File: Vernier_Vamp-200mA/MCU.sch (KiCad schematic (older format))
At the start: 11 parts

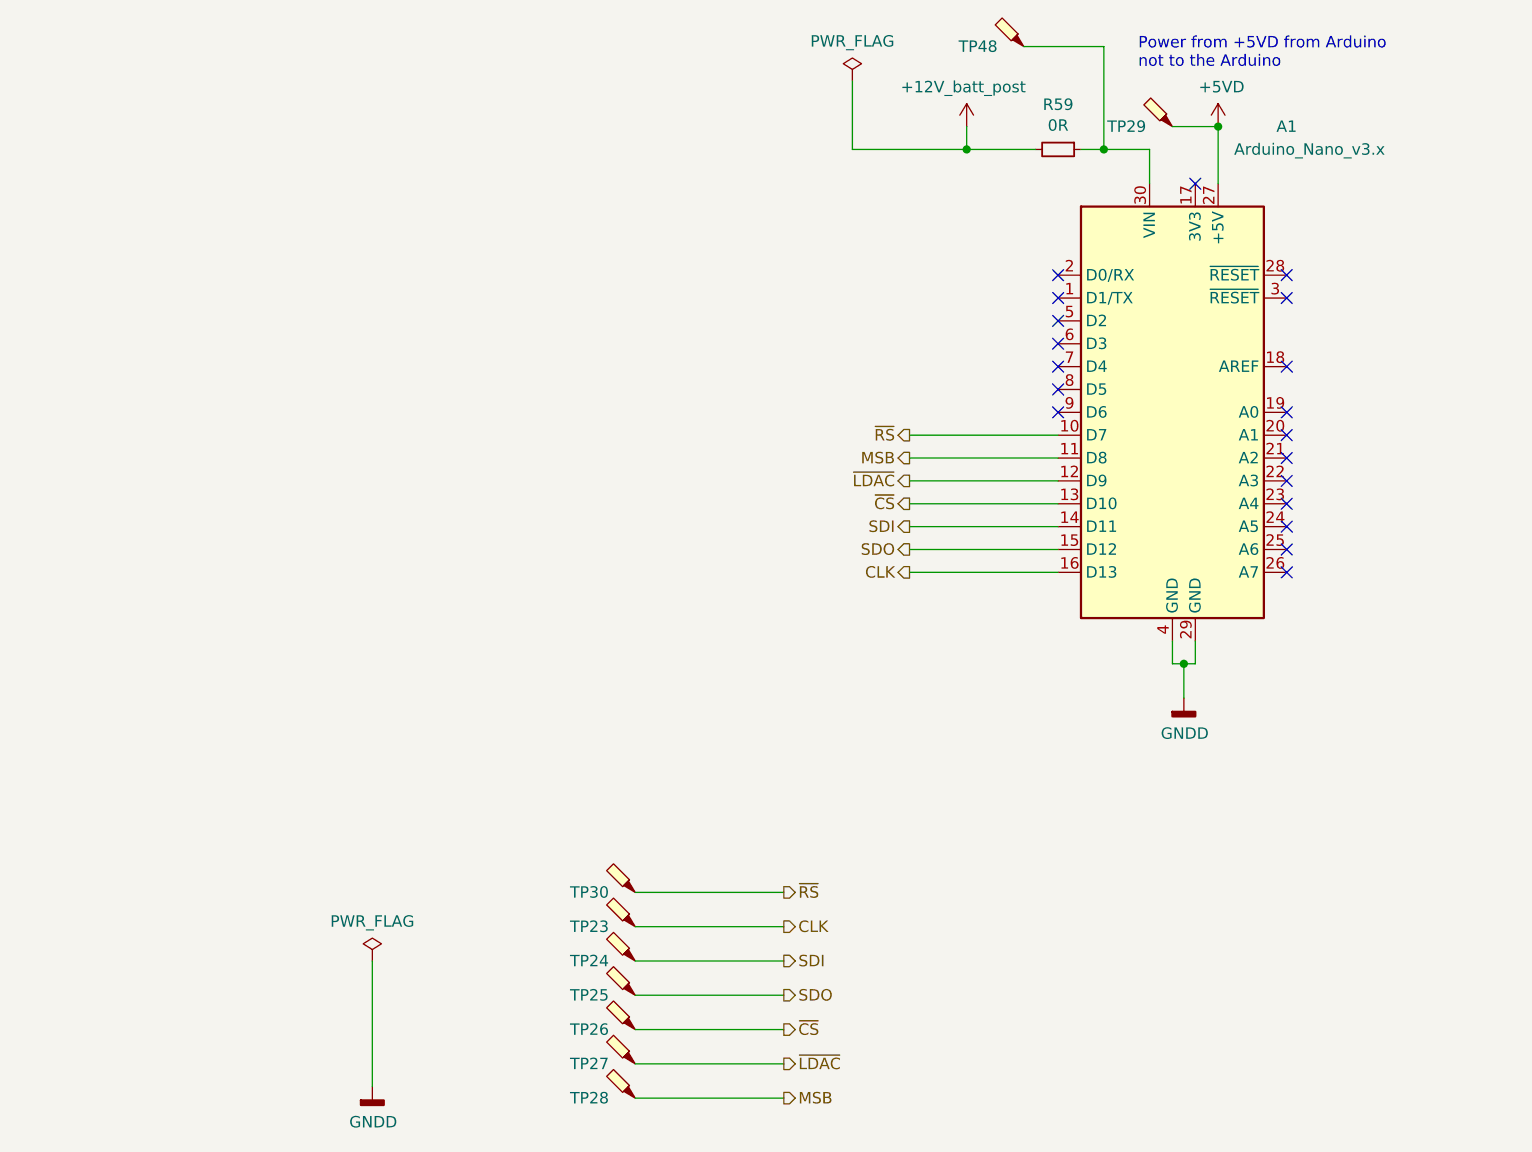
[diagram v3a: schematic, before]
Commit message: 1.0D Update
LCCD changes
-Addition of trigger for calibration
-PCB optimisation

HCCD changes
-New output stage designed
-Changes from 1.0C applied to HCCD
-New more optimised layout
-New shielding over analog section
-Addition of trigger for calibration

New symbols and footprint creation
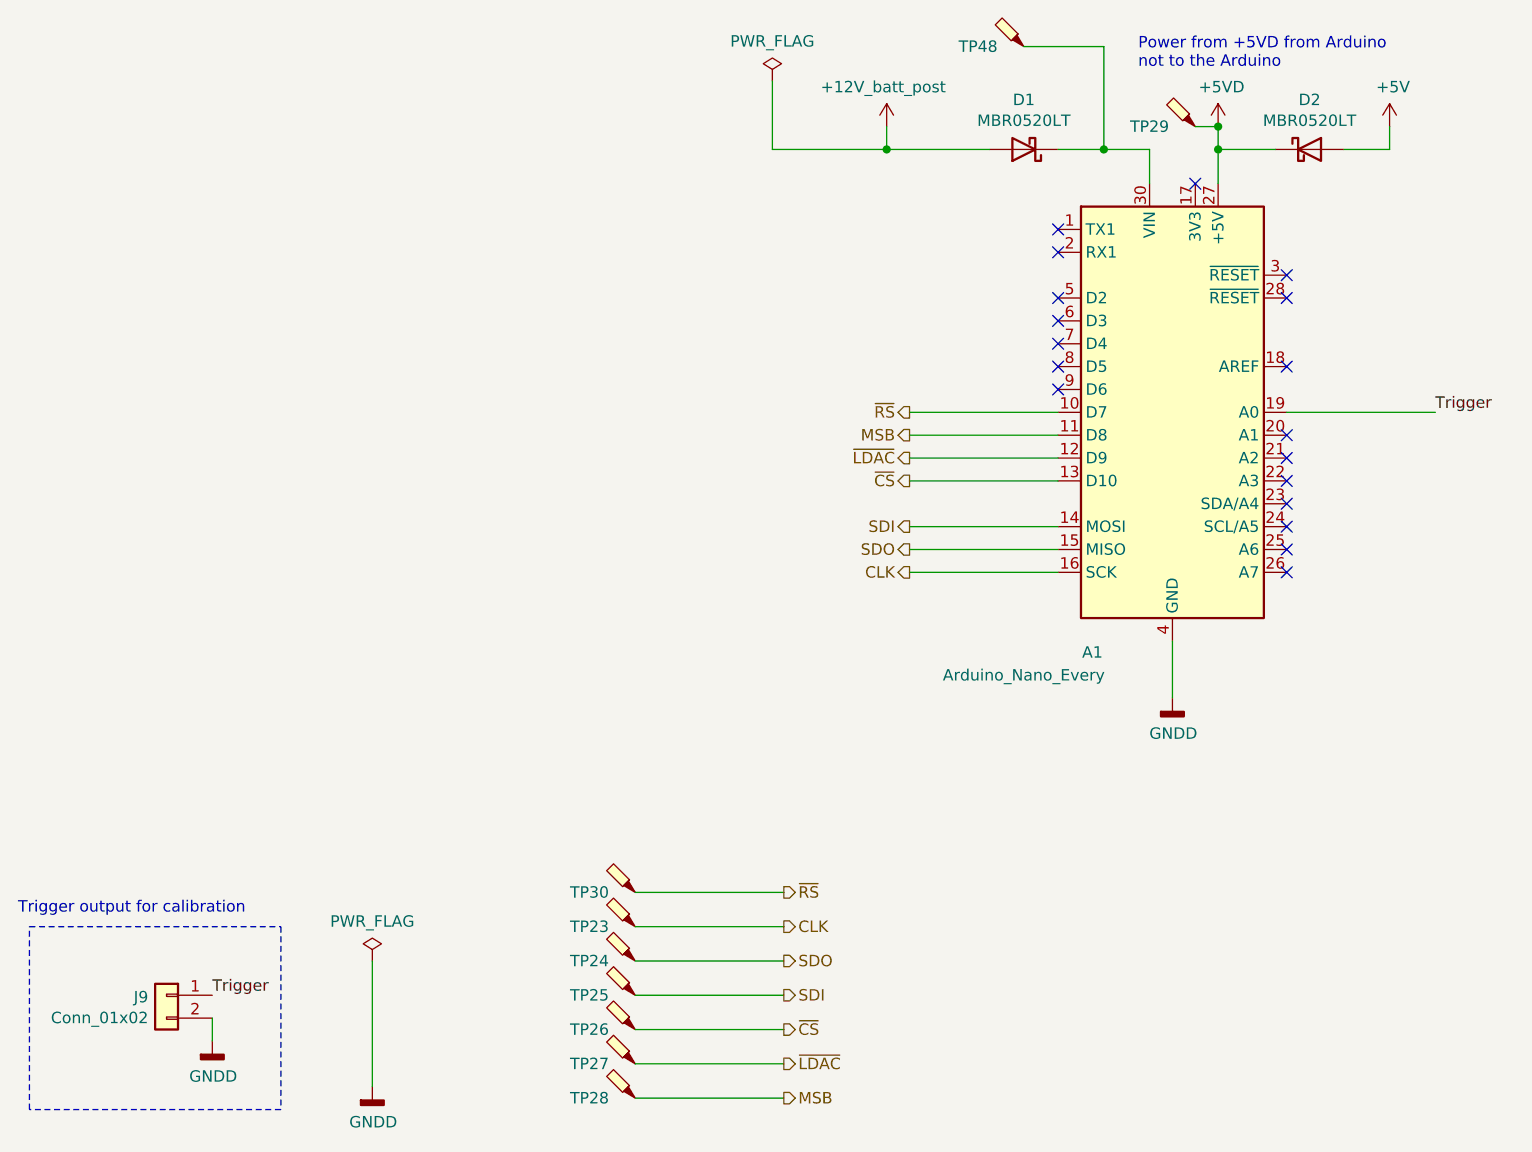
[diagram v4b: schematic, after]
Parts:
- removed A1: Arduino_Nano_v3.x, Module:Arduino_Nano, symbol MCU_Module:Arduino_Nano_v3.x
- removed R59: 0R, Resistor_SMD:R_0603_1608Metric_Pad1.05x0.95mm_HandSolder, symbol Device:R_Small
- added A1: Arduino_Nano_Every, Module:Arduino_Nano, symbol MCU_Module:Arduino_Nano_Every
- added D1, D2: MBR0520LT, Diode_SMD:D_SOD-123, symbol Diode:MBR0520LT
- added J9: Conn_01x02, Connector_PinHeader_2.54mm:PinHeader_1x02_P2.54mm_Vertical, symbol Connector_Generic:Conn_01x02
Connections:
- net +12V_batt_post: now also D1.2 (A)
- net +5VD: now also A1.27 (+5V), D2.1 (K)
- net CLK: now also A1.16 (SCK)
- net GNDD: now also A1.29 (GND), A1.4 (GND), J9.2 (Pin_2)
- net MSB: now also A1.11 (D8)
- net SDI: now also TP25.1, A1.14 (MOSI); no longer TP24.1
- net SDO: now also TP24.1, A1.15 (MISO); no longer TP25.1
- net ~CS: now also A1.13 (D10)
- net ~LDAC: now also A1.12 (D9)
- net ~RS: now also A1.10 (D7)
- net at TP48.1: now also A1.30 (VIN), D1.1 (K)
- new net +5V: D2.2 (A)
- new net Trigger: A1.19 (A0), J9.1 (Pin_1)
- no-connect marks 19 -> 18
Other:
- note added: "Trigger output for calibration"
- moved on the sheet: TP29
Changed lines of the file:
@@
 $Descr A4 11693 8268
 encoding utf-8
-Sheet 5 7
-Title "\"Vernier Vamp\" Coil Driver - 200mA"
+Sheet 4 7
+Title "\"Vernier Vamp\" Coil Driver - HCCD"
 Date "2020-04-27"
-Rev "1.0B"
+Rev "1.0D"
 Comp "Strathclyde University"
 Comment1 "Designed by: Marcin Mrozowski"
@@
 L power:GNDD #PWR0196
 U 1 1 5E449396
-P 5900 5050
+P 5850 5050
 AR Path="/5E1DEB8C/5E449396" Ref="#PWR0196"  Part="1"
 AR Path="/5E5EF2D7/5E449396" Ref="#PWR?"  Part="1"
-F 0 "#PWR0196" H 5900 4800 50  0001 C CNN
-F 1 "GNDD" H 5904 4895 50  0000 C CNN
-F 2 "" H 5900 5050 50  0001 C CNN
-F 3 "" H 5900 5050 50  0001 C CNN
-	1    5900 5050
-	1    0    0    -1
-$EndComp
-Wire Wire Line
-	5850 4800 5850 4900
-Wire Wire Line
-	5850 4900 5900 4900
-Wire Wire Line
-	5950 4900 5950 4800
-Wire Wire Line
-	5900 4900 5900 5050
-Connection ~ 5900 4900
-Wire Wire Line
-	5900 4900 5950 4900
+F 0 "#PWR0196" H 5850 4800 50  0001 C CNN
+F 1 "GNDD" H 5854 4895 50  0000 C CNN
+F 2 "" H 5850 5050 50  0001 C CNN
+F 3 "" H 5850 5050 50  0001 C CNN
+	1    5850 5050
+	1    0    0    -1
+$EndComp
+Wire Wire Line
+	5850 4800 5850 5050
 Text HLabel 4700 4500 0    50   Output ~ 0
 CLK
-Text HLabel 4700 4200 0    50   Output ~ 0
+Text HLabel 4700 4100 0    50   Output ~ 0
 ~CS
 Text HLabel 4700 4300 0    50   Output ~ 0
@@
 	5350 4500 4700 4500
 Wire Wire Line
-	4700 4200 5350 4200
+	4700 4100 5350 4100
 Wire Wire Line
 	4700 4300 5350 4300
 Wire Wire Line
 	4700 4400 5350 4400
-NoConn ~ 5350 3700
-NoConn ~ 5350 3600
-NoConn ~ 5350 3500
-NoConn ~ 5350 3400
-NoConn ~ 6350 3600
-NoConn ~ 6350 3800
-NoConn ~ 6350 3900
-NoConn ~ 6350 4000
-NoConn ~ 6350 4100
-NoConn ~ 6350 4200
-NoConn ~ 6350 4300
-NoConn ~ 6350 4400
-NoConn ~ 6350 4500
-Text HLabel 4700 4100 0    50   Output ~ 0
+Text HLabel 4700 4000 0    50   Output ~ 0
 ~LDAC
-Text HLabel 4700 4000 0    50   Output ~ 0
+Text HLabel 4700 3900 0    50   Output ~ 0
 MSB
-NoConn ~ 5350 3800
-Wire Wire Line
-	4700 4000 5350 4000
-Wire Wire Line
-	5350 4100 4700 4100
-Text HLabel 4700 3900 0    50   Output ~ 0
+Wire Wire Line
+	4700 3900 5350 3900
+Wire Wire Line
+	5350 4000 4700 4000
+Text HLabel 4700 3800 0    50   Output ~ 0
 ~RS
-NoConn ~ 5350 3200
-NoConn ~ 5350 3300
 NoConn ~ 5950 2800
 $Comp
@@
 Text HLabel 4150 6500 2    50   Output ~ 0
 ~CS
+Text HLabel 4150 6350 2    50   Output ~ 0
+SDI
 Text HLabel 4150 6200 2    50   Output ~ 0
-SDI
-Text HLabel 4150 6350 2    50   Output ~ 0
 SDO
 Wire Wire Line
@@
 	4150 6500 3500 6500
 Wire Wire Line
+	4150 6350 3500 6350
+Wire Wire Line
 	4150 6200 3500 6200
-Wire Wire Line
-	4150 6350 3500 6350
 Text HLabel 4150 6650 2    50   Output ~ 0
 ~LDAC
@@
 L Connector:TestPoint_Probe TP29
 U 1 1 62363521
-P 5850 2550
-F 0 "TP29" V 5850 2750 50  0000 C CNN
-F 1 "TestPoint_Probe" V 6049 2605 50  0001 C CNN
-F 2 "TestPoint:TestPoint_Pad_D1.0mm" H 6050 2550 50  0001 C CNN
-F 3 "~" H 6050 2550 50  0001 C CNN
-	1    5850 2550
-	0    -1   -1   0
-$EndComp
-Wire Wire Line
-	6050 2550 5850 2550
+P 5950 2550
+F 0 "TP29" V 5950 2750 50  0000 C CNN
+F 1 "TestPoint_Probe" V 6149 2605 50  0001 C CNN
+F 2 "TestPoint:TestPoint_Pad_D1.0mm" H 6150 2550 50  0001 C CNN
+F 3 "~" H 6150 2550 50  0001 C CNN
+	1    5950 2550
+	0    -1   -1   0
+$EndComp
+Wire Wire Line
+	6050 2550 5950 2550
 Connection ~ 6050 2550
-$Comp
-L MCU_Module:Arduino_Nano_v3.x A1
-U 1 1 5E447129
-P 5850 3800
-AR Path="/5E1DEB8C/5E447129" Ref="A1"  Part="1"
-AR Path="/5E5EF2D7/5E447129" Ref="A?"  Part="1"
-F 0 "A1" H 6350 5050 50  0000 C CNN
-F 1 "Arduino_Nano_v3.x" H 6450 4950 50  0000 C CNN
-F 2 "Module:Arduino_Nano" H 5850 3800 50  0001 C CIN
-F 3 "http://www.mouser.com/pdfdocs/Gravitech_Arduino_Nano3_0.pdf" H 5850 3800 50  0001 C CNN
-	1    5850 3800
-	1    0    0    -1
-$EndComp
-Wire Wire Line
-	6050 2550 6050 2800
+Wire Wire Line
+	6050 2550 6050 2650
 Wire Wire Line
 	5750 2800 5750 2650
@@
 $EndComp
 Wire Wire Line
-	4700 3900 5350 3900
+	4700 3800 5350 3800
 Text HLabel 4150 5900 2    50   Output ~ 0
 ~RS
@@
 	1    0    0    -1
 $EndComp
-NoConn ~ 6350 3200
-NoConn ~ 6350 3300
-Wire Wire Line
-	4950 2550 4950 2650
-Wire Wire Line
-	4950 2650 5250 2650
+Wire Wire Line
+	4600 2550 4600 2650
 $Comp
 L custom_power_rails:+12V_batt_post #PWR?
 U 1 1 5ECA4E39
-P 4950 2550
+P 4600 2550
 AR Path="/5E1DD6A9/5EA9C7F8/5ECA4E39" Ref="#PWR?"  Part="1"
 AR Path="/5E1DEB8C/5ECA4E39" Ref="#PWR0210"  Part="1"
-F 0 "#PWR0210" H 4950 2500 50  0001 C CNN
-F 1 "+12V_batt_post" H 4935 2723 50  0000 C CNN
-F 2 "" H 4950 2550 50  0001 C CNN
-F 3 "" H 4950 2550 50  0001 C CNN
-	1    4950 2550
+F 0 "#PWR0210" H 4600 2500 50  0001 C CNN
+F 1 "+12V_batt_post" H 4585 2723 50  0000 C CNN
+F 2 "" H 4600 2550 50  0001 C CNN
+F 3 "" H 4600 2550 50  0001 C CNN
+	1    4600 2550
 	1    0    0    -1
 $EndComp
@@
 L power:PWR_FLAG #FLG?
 U 1 1 5EA5082E
-P 4450 2350
+P 4100 2350
 AR Path="/5E1DD6A9/5EA5082E" Ref="#FLG?"  Part="1"
 AR Path="/5E1DD6A9/5E9C5630/5EA5082E" Ref="#FLG?"  Part="1"
 AR Path="/5E1DD6A9/5EA9C7F8/5EA5082E" Ref="#FLG?"  Part="1"
 AR Path="/5E1DEB8C/5EA5082E" Ref="#FLG0105"  Part="1"
-F 0 "#FLG0105" H 4450 2425 50  0001 C CNN
-F 1 "PWR_FLAG" H 4450 2523 50  0000 C CNN
-F 2 "" H 4450 2350 50  0001 C CNN
-F 3 "~" H 4450 2350 50  0001 C CNN
-	1    4450 2350
-	1    0    0    -1
-$EndComp
-Wire Wire Line
-	4950 2650 4450 2650
-Wire Wire Line
-	4450 2650 4450 2350
+F 0 "#FLG0105" H 4100 2425 50  0001 C CNN
+F 1 "PWR_FLAG" H 4100 2523 50  0000 C CNN
+F 2 "" H 4100 2350 50  0001 C CNN
+F 3 "~" H 4100 2350 50  0001 C CNN
+	1    4100 2350
+	1    0    0    -1
+$EndComp
+Wire Wire Line
+	4600 2650 4100 2650
+Wire Wire Line
+	4100 2650 4100 2350
 $Comp
 L Connector:TestPoint_Probe TP48
@@
 	0    -1   -1   0
 $EndComp
-$Comp
-L Device:R_Small R59
-U 1 1 5EB1CFC9
-P 5350 2650
-F 0 "R59" V 5154 2650 50  0000 C CNN
-F 1 "0R" V 5245 2650 50  0000 C CNN
-F 2 "Resistor_SMD:R_0603_1608Metric_Pad1.05x0.95mm_HandSolder" H 5350 2650 50  0001 C CNN
-F 3 "~" H 5350 2650 50  0001 C CNN
-	1    5350 2650
-	0    1    1    0
-$EndComp
-Connection ~ 4950 2650
+Connection ~ 4600 2650
 Wire Wire Line
 	5750 2650 5550 2650
@@
 	5200 2200 5550 2200
 Connection ~ 5550 2650
-Wire Wire Line
-	5550 2650 5450 2650
+$Comp
+L MCU_Module:Arduino_Nano_Every A1
+U 1 1 609E160A
+P 5850 3800
+F 0 "A1" H 5500 2750 50  0000 C CNN
+F 1 "Arduino_Nano_Every" H 5200 2650 50  0000 C CNN
+F 2 "Module:Arduino_Nano" H 5850 3800 50  0001 C CIN
+F 3 "https://content.arduino.cc/assets/NANOEveryV3.0_sch.pdf" H 5850 3800 50  0001 C CNN
+	1    5850 3800
+	1    0    0    -1
+$EndComp
+NoConn ~ 5350 3000
+NoConn ~ 5350 3100
+NoConn ~ 5350 3300
+NoConn ~ 5350 3400
+NoConn ~ 5350 3500
+NoConn ~ 5350 3600
+NoConn ~ 6350 3600
+NoConn ~ 6350 3200
+NoConn ~ 6350 3300
+NoConn ~ 6350 3900
+NoConn ~ 6350 4000
+NoConn ~ 6350 4100
+NoConn ~ 6350 4200
+NoConn ~ 6350 4300
+NoConn ~ 6350 4400
+NoConn ~ 6350 4500
+$Comp
+L Connector_Generic:Conn_01x02 J9
+U 1 1 609F0648
+P 1450 6350
+F 0 "J9" H 1530 6342 50  0000 L CNN
+F 1 "Conn_01x02" H 1530 6251 50  0000 L CNN
+F 2 "Connector_PinHeader_2.54mm:PinHeader_1x02_P2.54mm_Vertical" H 1450 6350 50  0001 C CNN
+F 3 "~" H 1450 6350 50  0001 C CNN
+	1    1450 6350
+	-1   0    0    -1
+$EndComp
+Wire Wire Line
+	7000 3800 6350 3800
+Text Label 7000 3800 0    50   ~ 0
+Trigger
+Text Label 1650 6350 0    50   ~ 0
+Trigger
+$Comp
+L power:GNDD #PWR02
+U 1 1 609F6AB5
+P 1650 6550
+AR Path="/5E1DEB8C/609F6AB5" Ref="#PWR02"  Part="1"
+AR Path="/5E5EF2D7/609F6AB5" Ref="#PWR?"  Part="1"
+F 0 "#PWR02" H 1650 6300 50  0001 C CNN
+F 1 "GNDD" H 1654 6395 50  0000 C CNN
+F 2 "" H 1650 6550 50  0001 C CNN
+F 3 "" H 1650 6550 50  0001 C CNN
+	1    1650 6550
+	1    0    0    -1
+$EndComp
+Wire Wire Line
+	1650 6450 1650 6550
+$Comp
+L Diode:MBR0520LT D1
+U 1 1 609F92F2
+P 5200 2650
+F 0 "D1" H 5200 2433 50  0000 C CNN
+F 1 "MBR0520LT" H 5200 2524 50  0000 C CNN
+F 2 "Diode_SMD:D_SOD-123" H 5200 2475 50  0001 C CNN
+F 3 "http://www.onsemi.com/pub_link/Collateral/MBR0520LT1-D.PDF" H 5200 2650 50  0001 C CNN
+	1    5200 2650
+	-1   0    0    1
+$EndComp
+$Comp
+L power:+5V #PWR03
+U 1 1 609FD6B4
+P 6800 2550
+F 0 "#PWR03" H 6800 2400 50  0001 C CNN
+F 1 "+5V" H 6815 2723 50  0000 C CNN
+F 2 "" H 6800 2550 50  0001 C CNN
+F 3 "" H 6800 2550 50  0001 C CNN
+	1    6800 2550
+	1    0    0    -1
+$EndComp
+$Comp
+L Diode:MBR0520LT D2
+U 1 1 60A035A3
+P 6450 2650
+F 0 "D2" H 6450 2867 50  0000 C CNN
+F 1 "MBR0520LT" H 6450 2776 50  0000 C CNN
+F 2 "Diode_SMD:D_SOD-123" H 6450 2475 50  0001 C CNN
+F 3 "http://www.onsemi.com/pub_link/Collateral/MBR0520LT1-D.PDF" H 6450 2650 50  0001 C CNN
+	1    6450 2650
+	1    0    0    -1
+$EndComp
+Wire Wire Line
+	6800 2550 6800 2650
+Wire Wire Line
+	6800 2650 6600 2650
+Wire Wire Line
+	6300 2650 6050 2650
+Connection ~ 6050 2650
+Wire Wire Line
+	6050 2650 6050 2800
+Wire Wire Line
+	5350 2650 5550 2650
+Wire Wire Line
+	4600 2650 5050 2650
+Wire Notes Line
+	1950 6050 1950 6850
+Wire Notes Line
+	1950 6850 850  6850
+Wire Notes Line
+	850  6850 850  6050
+Wire Notes Line
+	850  6050 1950 6050
+Text Notes 800  6000 0    50   ~ 0
+Trigger output for calibration
+NoConn ~ 5350 3700
 $EndSCHEMATC
